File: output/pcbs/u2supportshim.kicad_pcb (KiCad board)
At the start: 2 copper layers, 145.2 x 18.3 mm, 3 parts

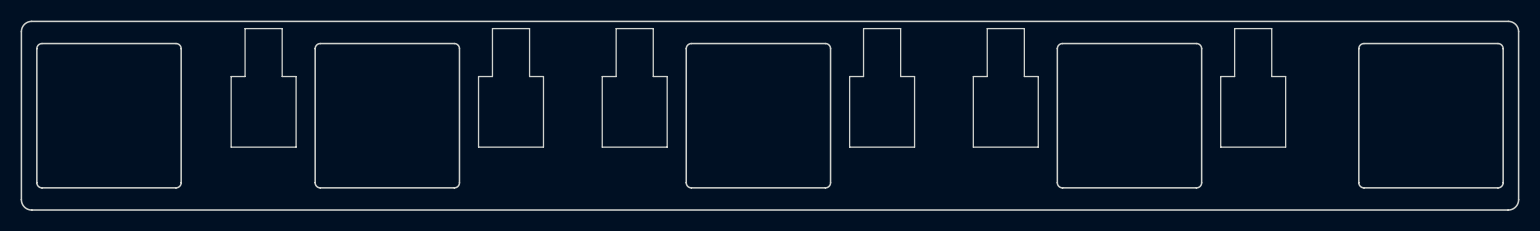
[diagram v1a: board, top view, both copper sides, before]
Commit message: Fixed Pinouts.
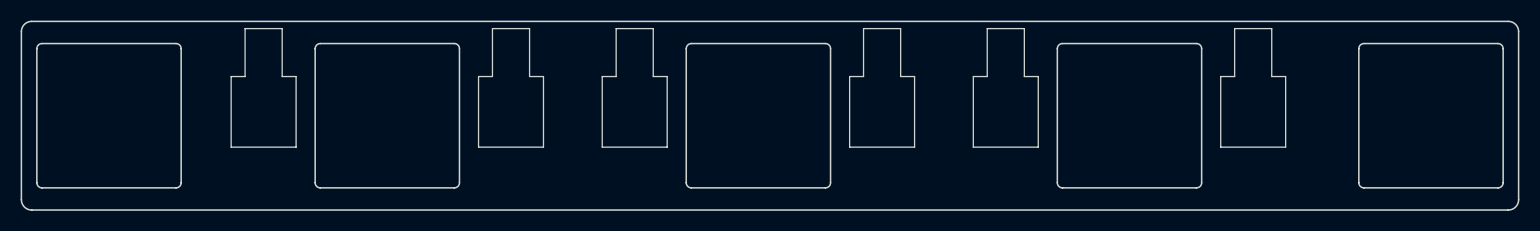
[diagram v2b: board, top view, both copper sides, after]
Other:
- net class Default added: clearance 0.2, trace_width 0.25, via_dia 0.8, via_drill 0.4
- board text removed: "JLCJLCJLCJLC"
